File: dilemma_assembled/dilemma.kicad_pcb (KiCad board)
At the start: 2 copper layers, 134 x 95.1 mm, 122 parts, among them J1 USB_C_Receptacle_USB2.0, J102 Serial, J103 Serial, J104 Conn_01x02_Female, J107 Conn_01x08_Female, J108 Conn_01x01_Female, J109 Conn_01x01_Female, J113 Cirque, J5 Conn_01x02, SW1 SW_Push, SW101 SW_Push, SW102 SW_Push, SW103 SW_Push, SW104 SW_Push, SW105 SW_Push, SW106 SW_Push, SW107 SW_Push, SW108 SW_Push, SW109 SW_Push, SW110 SW_SPST, SW111 SW_SPST, SW112 SW_Push, SW113 SW_Push, SW114 SW_Push, SW115 SW_Push, SW116 SW_Push, SW117 SW_Push, SW118 SW_Push, SW119 locked, SW2 SW_Push, U1 RP2040, U2 GD25Q80CEIGR, U3 XC6210B332MR-G, Y1 Crystal_GND24

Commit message: silkscreen
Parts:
- moved kibuzzard-62C19A64 4.98 mm to (174.0, 57.8) (x2)
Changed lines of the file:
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@@
   )
   (footprint "kibuzzard-62C19A64" (layer "F.Cu")
-    (at 173.985 52.82)
+    (at 173.98 57.797244)
     (descr "Converted using: scripting")
     (tags "svg2mod")
@@
       ) (layer "B.SilkS") (width 0) (fill solid))
     (fp_poly (pts
-        (xy -0.628572 -0.228829)
-        (xy -2.514286 -0.228829)
-        (xy -2.514286 0.228829)
-        (xy -0.628572 0.228829)
+        (xy 8.13087 1.848914)
+        (xy 8.43612 1.758178)
+        (xy 8.707402 1.625279)
+        (xy 8.894434 1.491623)
+        (xy 9.078806 1.319801)
+        (xy 9.24415 1.127186)
+        (xy 9.374101 0.931151)
+        (xy 9.391077 0.899545)
+        (xy 9.443301 0.798144)
+        (xy 9.486513 0.709993)
+        (xy 9.52162 0.628475)
+        (xy 9.549533 0.546973)
+        (xy 9.57116 0.45887)
+        (xy 9.587411 0.357551)
+        (xy 9.599194 0.236398)
+        (xy 9.607419 0.088794)
+        (xy 9.612995 -0.091877)
+        (xy 9.616831 -0.312231)
+        (xy 9.619837 -0.578886)
+        (xy 9.621768 -0.779448)
+        (xy 9.632643 -1.916441)
+        (xy 9.205177 -1.916441)
+        (xy 9.193266 -0.822353)
+        (xy 9.190027 -0.540714)
+        (xy 9.186811 -0.310115)
+        (xy 9.183271 -0.12439)
+        (xy 9.179061 0.022626)
+        (xy 9.173832 0.137099)
+        (xy 9.167239 0.225196)
+        (xy 9.158935 0.29308)
+        (xy 9.148572 0.346919)
+        (xy 9.135804 0.392879)
+        (xy 9.122772 0.43043)
+        (xy 8.994483 0.711604)
+        (xy 8.833277 0.946821)
+        (xy 8.636978 1.138348)
+        (xy 8.40341 1.288452)
+        (xy 8.222881 1.36776)
+        (xy 7.961866 1.435914)
+        (xy 7.698677 1.451174)
+        (xy 7.439784 1.417192)
+        (xy 7.19166 1.337621)
+        (xy 6.960775 1.216115)
+        (xy 6.753603 1.056328)
+        (xy 6.576613 0.861913)
+        (xy 6.436279 0.636523)
+        (xy 6.339072 0.383812)
+        (xy 6.316885 0.291779)
+        (xy 6.308163 0.218751)
+        (xy 6.300685 0.093322)
+        (xy 6.294577 -0.079712)
+        (xy 6.289966 -0.295557)
+        (xy 6.286979 -0.549416)
+        (xy 6.285741 -0.836495)
+        (xy 6.285714 -0.888119)
+        (xy 6.285714 -1.916441)
+        (xy 5.857143 -1.916441)
+        (xy 5.857143 -0.83408)
+        (xy 5.857644 -0.521866)
+        (xy 5.859712 -0.260206)
+        (xy 5.864191 -0.042451)
+        (xy 5.871928 0.138047)
+        (xy 5.883768 0.287937)
+        (xy 5.900556 0.413868)
+        (xy 5.923138 0.522487)
+        (xy 5.95236 0.620445)
+        (xy 5.989066 0.714389)
+        (xy 6.034103 0.810968)
+        (xy 6.077068 0.895307)
+        (xy 6.209442 1.102579)
+        (xy 6.383106 1.304709)
+        (xy 6.583016 1.486948)
+        (xy 6.79413 1.634545)
+        (xy 6.877518 1.680167)
+        (xy 7.182599 1.802501)
+        (xy 7.497555 1.871272)
+        (xy 7.81583 1.886678)
       ) (layer "B.SilkS") (width 0) (fill solid))
     (fp_poly (pts
@@
       ) (layer "B.SilkS") (width 0) (fill solid))
     (fp_poly (pts
-        (xy 8.13087 1.848914)
-        (xy 8.43612 1.758178)
-        (xy 8.707402 1.625279)
-        (xy 8.894434 1.491623)
-        (xy 9.078806 1.319801)
-        (xy 9.24415 1.127186)
-        (xy 9.374101 0.931151)
-        (xy 9.391077 0.899545)
-        (xy 9.443301 0.798144)
-        (xy 9.486513 0.709993)
-        (xy 9.52162 0.628475)
-        (xy 9.549533 0.546973)
-        (xy 9.57116 0.45887)
-        (xy 9.587411 0.357551)
-        (xy 9.599194 0.236398)
-        (xy 9.607419 0.088794)
-        (xy 9.612995 -0.091877)
-        (xy 9.616831 -0.312231)
-        (xy 9.619837 -0.578886)
-        (xy 9.621768 -0.779448)
-        (xy 9.632643 -1.916441)
-        (xy 9.205177 -1.916441)
-        (xy 9.193266 -0.822353)
-        (xy 9.190027 -0.540714)
-        (xy 9.186811 -0.310115)
-        (xy 9.183271 -0.12439)
-        (xy 9.179061 0.022626)
-        (xy 9.173832 0.137099)
-        (xy 9.167239 0.225196)
-        (xy 9.158935 0.29308)
-        (xy 9.148572 0.346919)
-        (xy 9.135804 0.392879)
-        (xy 9.122772 0.43043)
-        (xy 8.994483 0.711604)
-        (xy 8.833277 0.946821)
-        (xy 8.636978 1.138348)
-        (xy 8.40341 1.288452)
-        (xy 8.222881 1.36776)
-        (xy 7.961866 1.435914)
-        (xy 7.698677 1.451174)
-        (xy 7.439784 1.417192)
-        (xy 7.19166 1.337621)
-        (xy 6.960775 1.216115)
-        (xy 6.753603 1.056328)
-        (xy 6.576613 0.861913)
-        (xy 6.436279 0.636523)
-        (xy 6.339072 0.383812)
-        (xy 6.316885 0.291779)
-        (xy 6.308163 0.218751)
-        (xy 6.300685 0.093322)
-        (xy 6.294577 -0.079712)
-        (xy 6.289966 -0.295557)
-        (xy 6.286979 -0.549416)
-        (xy 6.285741 -0.836495)
-        (xy 6.285714 -0.888119)
-        (xy 6.285714 -1.916441)
-        (xy 5.857143 -1.916441)
-        (xy 5.857143 -0.83408)
-        (xy 5.857644 -0.521866)
-        (xy 5.859712 -0.260206)
-        (xy 5.864191 -0.042451)
-        (xy 5.871928 0.138047)
-        (xy 5.883768 0.287937)
-        (xy 5.900556 0.413868)
-        (xy 5.923138 0.522487)
-        (xy 5.95236 0.620445)
-        (xy 5.989066 0.714389)
-        (xy 6.034103 0.810968)
-        (xy 6.077068 0.895307)
-        (xy 6.209442 1.102579)
-        (xy 6.383106 1.304709)
-        (xy 6.583016 1.486948)
-        (xy 6.79413 1.634545)
-        (xy 6.877518 1.680167)
-        (xy 7.182599 1.802501)
-        (xy 7.497555 1.871272)
-        (xy 7.81583 1.886678)
+        (xy -0.628572 -0.228829)
+        (xy -2.514286 -0.228829)
+        (xy -2.514286 0.228829)
+        (xy -0.628572 0.228829)
       ) (layer "B.SilkS") (width 0) (fill solid))
     (fp_poly (pts
@@
   )
   (footprint "kibuzzard-62C19A64" (layer "B.Cu")
-    (at 174.035 52.82 180)
+    (at 174.03 57.797244 180)
     (descr "Converted using: scripting")
     (tags "svg2mod")
@@
     )
     (fp_poly (pts
-        (xy 0.086816 0.017363)
-        (xy 0.253008 0.017363)
-        (xy 0.318043 0.026045)
-        (xy 0.365559 0.05209)
-        (xy 0.394627 0.094258)
-        (xy 0.404316 0.151309)
-        (xy 0.39455 0.211305)
-        (xy 0.365249 0.258589)
-        (xy 0.31874 0.289595)
-        (xy 0.257349 0.300757)
-        (xy 0.086816 0.300757)
-        (xy 0.086816 0.017363)
-      ) (layer "B.SilkS") (width 0) (fill solid))
-    (fp_poly (pts
         (xy -0.917773 0.728431)
         (xy -0.798401 0.393077)
@@
         (xy -0.917773 0.728431)
       ) (layer "B.SilkS") (width 0) (fill solid))
+    (fp_poly (pts
+        (xy 0.086816 0.017363)
+        (xy 0.253008 0.017363)
+        (xy 0.318043 0.026045)
+        (xy 0.365559 0.05209)
+        (xy 0.394627 0.094258)
+        (xy 0.404316 0.151309)
+        (xy 0.39455 0.211305)
+        (xy 0.365249 0.258589)
+        (xy 0.31874 0.289595)
+        (xy 0.257349 0.300757)
+        (xy 0.086816 0.300757)
+        (xy 0.086816 0.017363)
+      ) (layer "B.SilkS") (width 0) (fill solid))
   )
   (gr_poly
@@
     (effects (font (size 0.8 0.8) (thickness 0.12)) (justify mirror))
   )
-  (gr_text "GND" (at 173.086667 56.98) (layer "B.SilkS")
+  (gr_text "GND" (at 173.083334 60.46) (layer "B.SilkS")
     (effects (font (size 0.7 0.7) (thickness 0.12)) (justify mirror))
   )
@@
     (effects (font (size 0.8 0.8) (thickness 0.12)) (justify mirror))
   )
-  (gr_text "5V" (at 173.52 59.36) (layer "B.SilkS")
+  (gr_text "5V" (at 173.516667 62.84) (layer "B.SilkS")
     (effects (font (size 0.7 0.7) (thickness 0.12)) (justify mirror))
   )
@@
     (effects (font (size 0.8 0.8) (thickness 0.12)))
   )
-  (gr_text "5V" (at 173.523333 59.34) (layer "F.SilkS")
+  (gr_text "5V" (at 173.52 62.82) (layer "F.SilkS")
     (effects (font (size 0.7 0.7) (thickness 0.12)))
   )
@@
     (effects (font (size 0.8 0.8) (thickness 0.12)))
   )
-  (gr_text "GND" (at 173.09 56.96) (layer "F.SilkS")
+  (gr_text "GND" (at 173.086667 60.44) (layer "F.SilkS")
     (effects (font (size 0.7 0.7) (thickness 0.12)))
   )

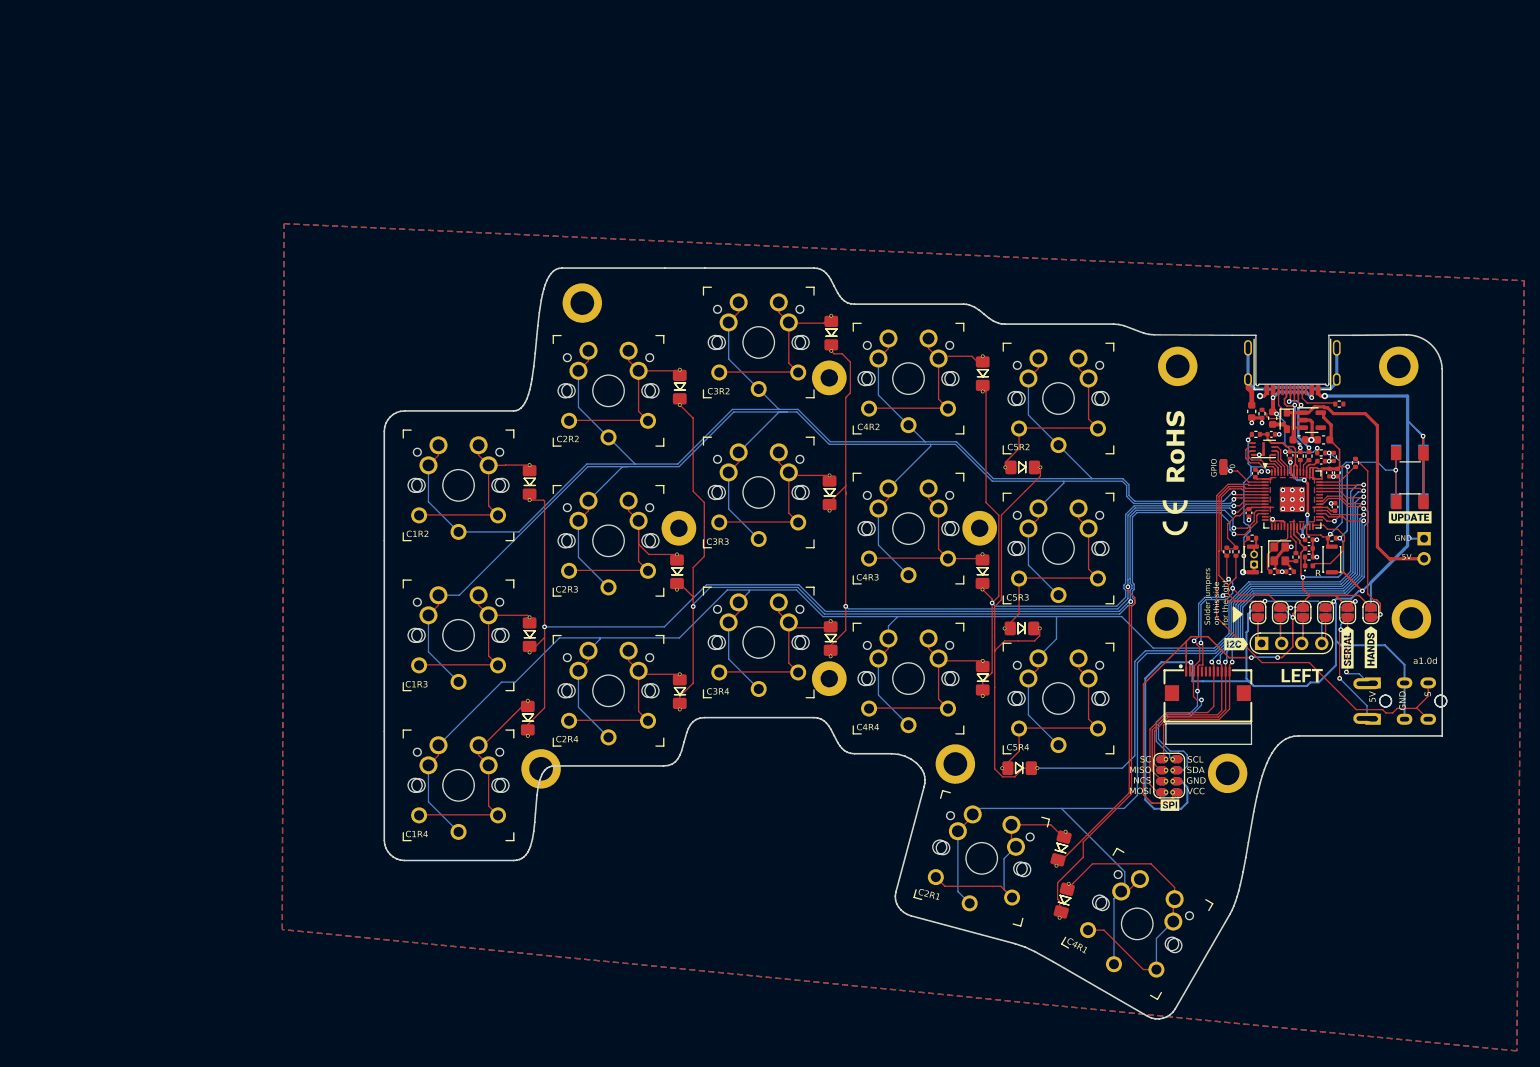
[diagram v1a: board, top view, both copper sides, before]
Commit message: add debug headers
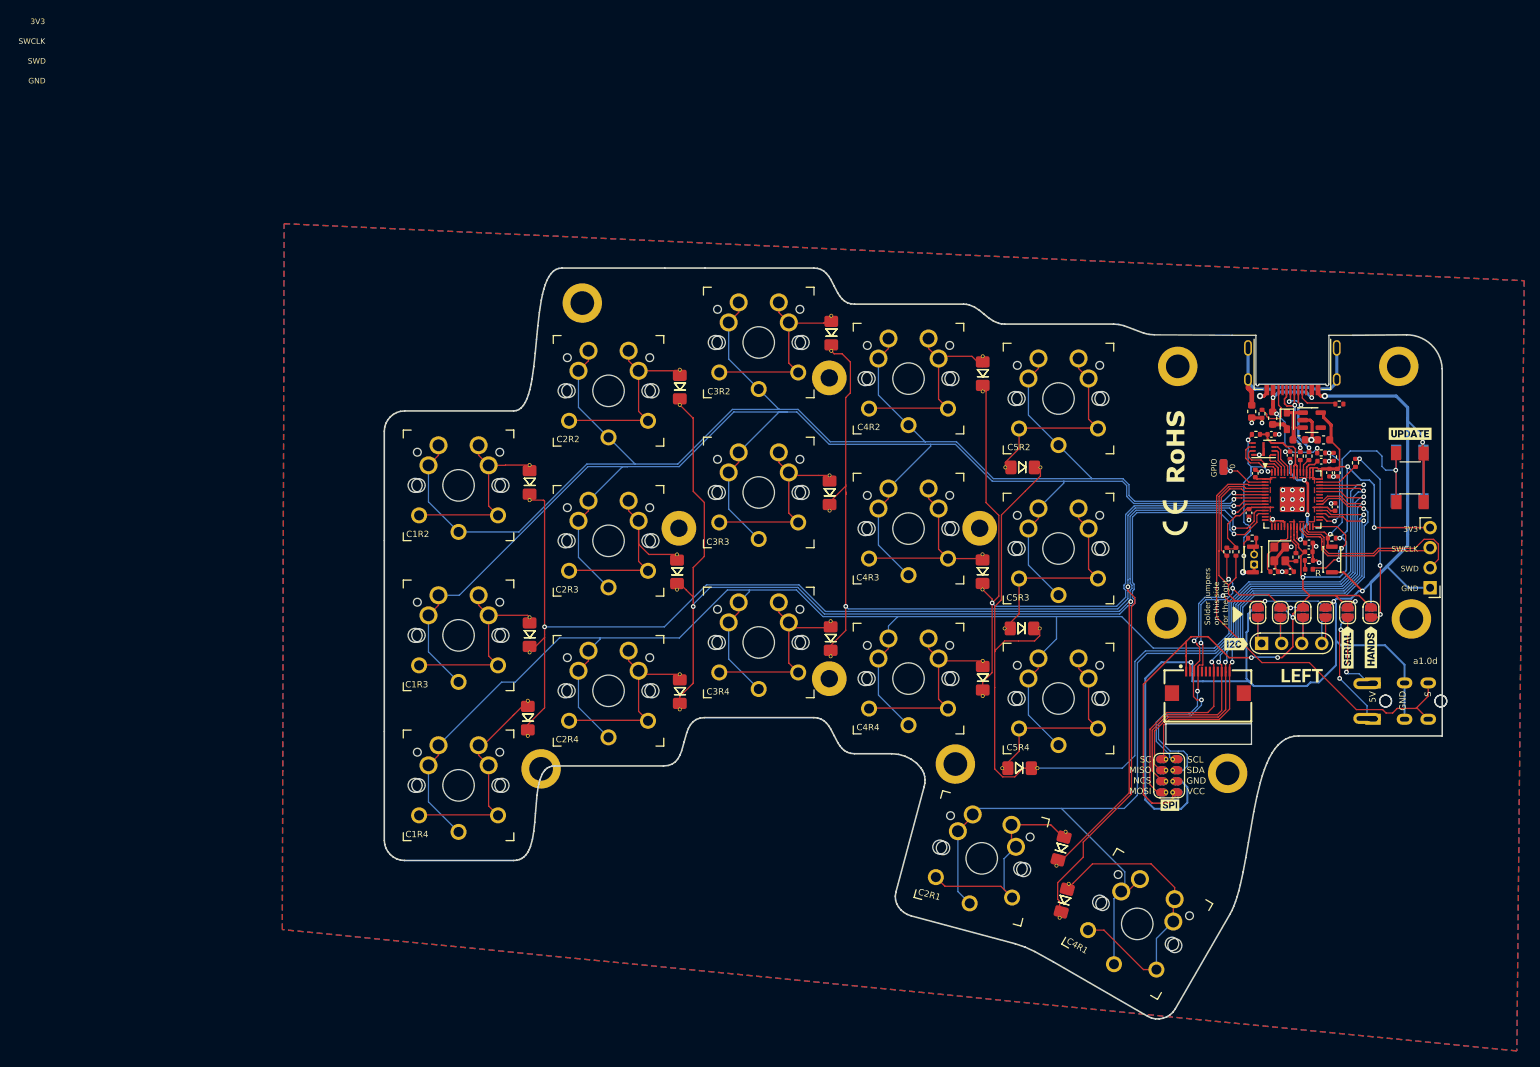
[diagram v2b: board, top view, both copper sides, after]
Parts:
- removed J104: Conn_01x02_Female, local-libraries:PinHeader_1x02_P2.54mm_Vertical
- added J105: Conn_01x04_Female, local-libraries:PinHeader_1x04_P2.54mm_Vertical_debug, F.Cu at (176.5, 59.1)
- moved kibuzzard-62C19A64 10.6 mm to (174.0, 47.2) (x2)
- moved D1 0.44 mm to (161.2, 64.4)
- moved C14 0.43 mm to (161.1, 62.2)
- moved R1 0.42 mm to (161.2, 63.3)
- moved C8 0.41 mm to (161.2, 61.0)
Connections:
- U1 pad 24: unconnected-(U1-Pad24) -> /SWCLK
- U1 pad 25: unconnected-(U1-Pad25) -> /SWD
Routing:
- net bat_l: track 39.4 -> 6.71 mm
- net /SWD: track 0.00 -> 24.1 mm
- net /SWCLK: track 0.00 -> 19.6 mm
- net +3V3: track 146.8 -> 164.4 mm, vias 7 -> 8
- net Gnd_l: track 196.6 -> 199.8 mm
- net Rst_l: track 35.7 -> 37.5 mm
- net +1V1: track 18.4 -> 19.5 mm
- net /LED: track 11.3 -> 11.9 mm, vias 0 -> 2
- net Net-(JP111-Pad1): track 24.0 -> 24.1 mm, vias 1 -> 3
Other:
- board text added: "3V3"
- board text added: "SWCLK"
- board text added: "SWD"

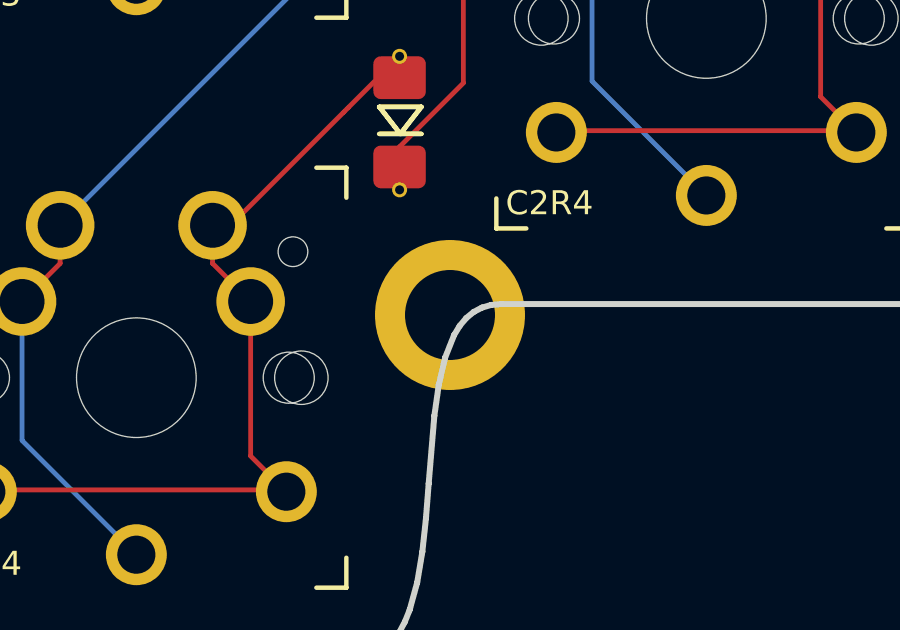
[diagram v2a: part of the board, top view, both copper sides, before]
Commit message: remove half plate screw
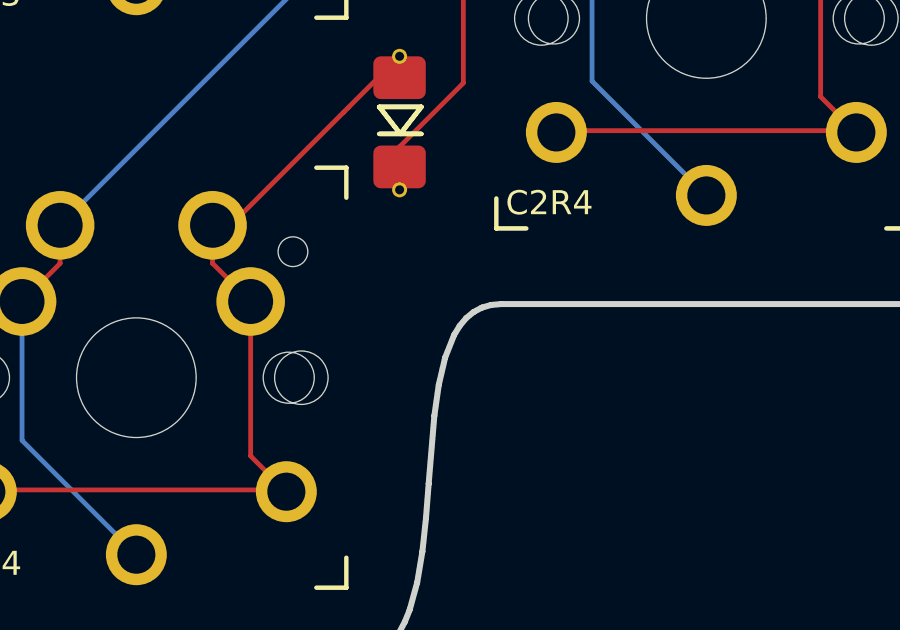
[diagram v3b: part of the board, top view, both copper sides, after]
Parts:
- removed H103: M4, local-libraries:MountingHole_3mm_Pad_thin
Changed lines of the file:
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@@
       (net 61 "Net-(D116-Pad2)") (pinfunction "A") (pintype "passive"))
-  )
-  (footprint "local-libraries:MountingHole_3mm_Pad_thin" (layer "F.Cu")
-    (at 63.88 89.6575)
-    (descr "Mounting Hole 3mm")
-    (tags "mounting hole 3mm")
-    (property "Sheetfile" "dilemma.kicad_sch")
-    (property "Sheetname" "")
-    (attr exclude_from_pos_files)
-    (fp_text reference "H103" (at 0 -4) (layer "F.SilkS") hide
-      (effects (font (size 1 1) (thickness 0.15)))
-    )
-    (fp_text value "M4" (at 0 4) (layer "F.Fab")
-      (effects (font (size 1 1) (thickness 0.15)))
-    )
-    (fp_text user "${REFERENCE}" (at 0 0) (layer "F.Fab")
-      (effects (font (size 1 1) (thickness 0.15)))
-    )
-    (fp_circle (center 0 0) (end 3 0) (layer "Cmts.User") (width 0.15) (fill none))
-    (fp_circle (center 0 0) (end 3.25 0) (layer "F.CrtYd") (width 0.05) (fill none))
-    (pad "1" thru_hole circle (at 0 0) (size 5 5) (drill 3) (layers *.Cu *.Mask)
-      (net 1 "Gnd_l") (pinfunction "1") (pintype "input"))
   )
   (footprint "local-libraries:D_1206_handsolder_reversible" (layer "F.Cu")
